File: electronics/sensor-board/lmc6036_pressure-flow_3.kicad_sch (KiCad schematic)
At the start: 13 parts

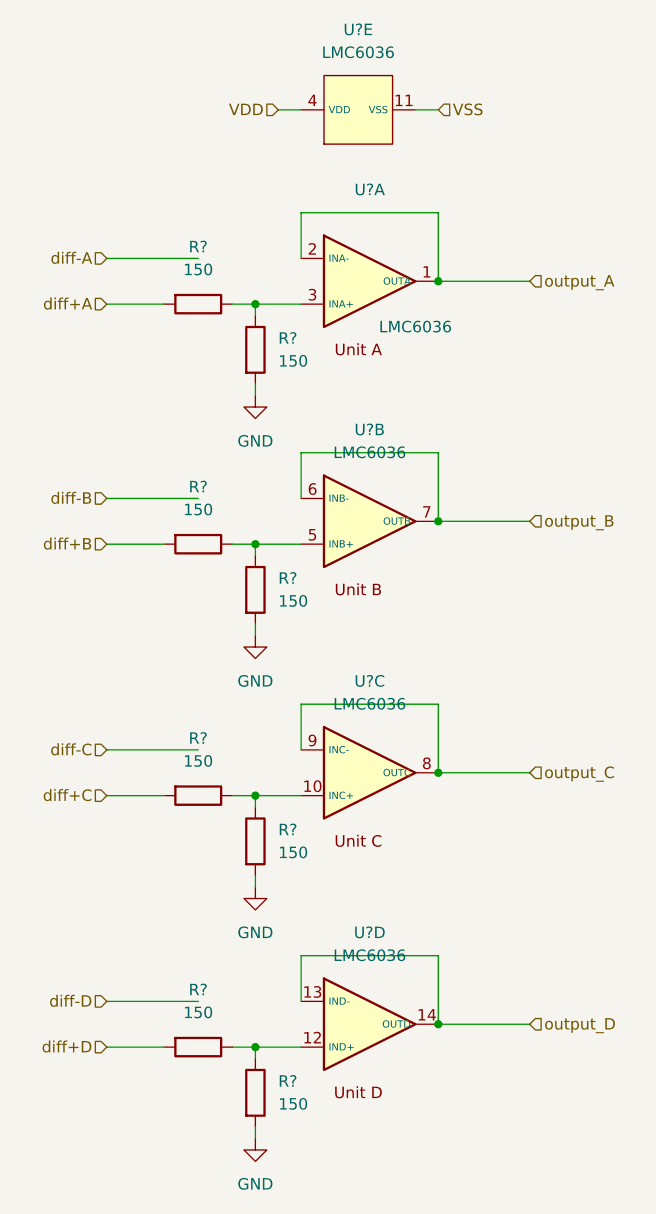
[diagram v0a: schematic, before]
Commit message: work on sensor-board
added MCP960 footprint
finished MCP960 array schematic
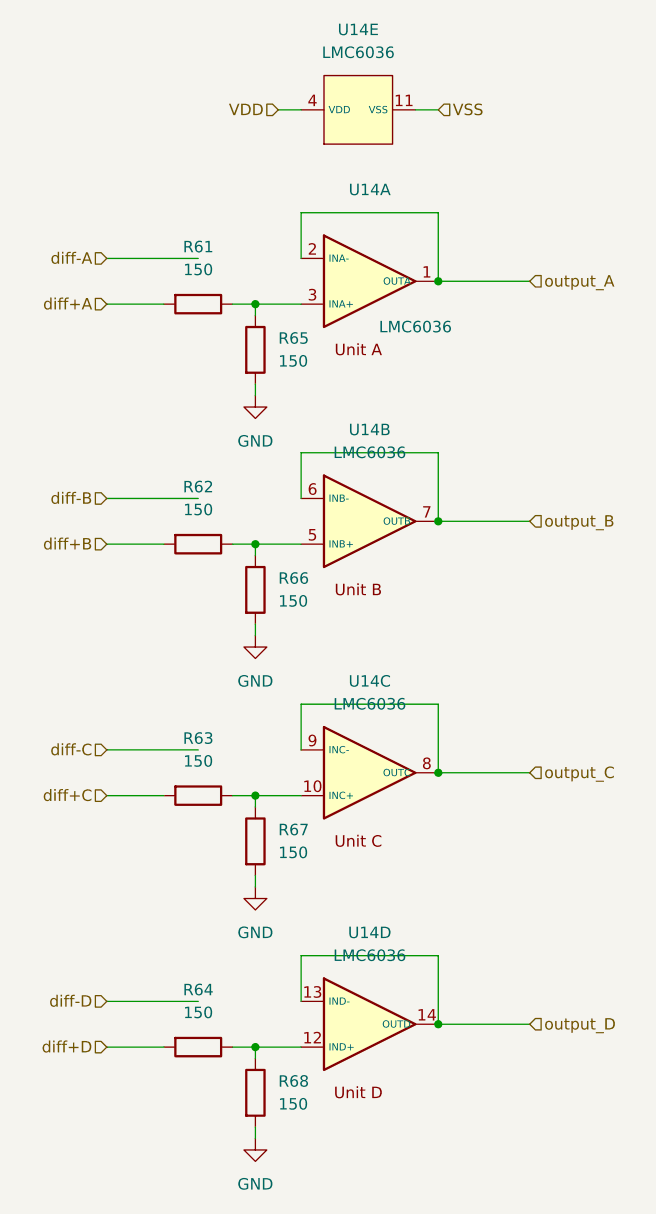
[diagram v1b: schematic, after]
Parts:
- removed R? (x8): 150, symbol Device:R
- removed U? (x5): LMC6036, LMC6036:SOP65P640X120-14N, symbol LMC6036_custom:LMC6036
- added R61, R62, R63, R64, R65, R66, R67, R68: 150, Resistor_SMD:R_0603_1608Metric, symbol Device:R
- added U14: LMC6036, LMC6036:SOP65P640X120-14N, symbol LMC6036_custom:LMC6036
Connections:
- net GND: now also R65.2, R66.2, R67.2, R68.2
- net VDD: now also U14.4 (VDD)
- net VSS: now also U14.11 (VSS)
- net diff+A: now also R61.2
- net diff+B: now also R62.2
- net diff+C: now also R63.2
- net diff+D: now also R64.2
- net output_A: now also U14.1 (OUTA), U14.2 (INA-)
- net output_B: now also U14.6 (INB-), U14.7 (OUTB)
- net output_C: now also U14.8 (OUTC), U14.9 (INC-)
- net output_D: now also U14.13 (IND-), U14.14 (OUTD)
- new net: R62.1, R66.1, U14.5 (INB+)
- new net: R64.1, R68.1, U14.12 (IND+)
- new net: R63.1, R67.1, U14.10 (INC+)
- new net: R61.1, R65.1, U14.3 (INA+)
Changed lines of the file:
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@@
   (symbol (lib_id "power:GND") (at 142.24 76.2 0) (unit 1)
     (in_bom yes) (on_board yes) (fields_autoplaced)
-    (property "Reference" "#PWR?" (id 0) (at 142.24 82.55 0)
+    (property "Reference" "#PWR0185" (id 0) (at 142.24 82.55 0)
       (effects (font (size 1.27 1.27)) hide)
     )
@@
   (symbol (lib_id "power:GND") (at 142.24 102.87 0) (unit 1)
     (in_bom yes) (on_board yes) (fields_autoplaced)
-    (property "Reference" "#PWR?" (id 0) (at 142.24 109.22 0)
+    (property "Reference" "#PWR0187" (id 0) (at 142.24 109.22 0)
       (effects (font (size 1.27 1.27)) hide)
     )
@@
   (symbol (lib_id "power:GND") (at 142.24 130.81 0) (unit 1)
     (in_bom yes) (on_board yes) (fields_autoplaced)
-    (property "Reference" "#PWR?" (id 0) (at 142.24 137.16 0)
+    (property "Reference" "#PWR0186" (id 0) (at 142.24 137.16 0)
       (effects (font (size 1.27 1.27)) hide)
     )
@@
   (symbol (lib_id "power:GND") (at 142.24 158.75 0) (unit 1)
     (in_bom yes) (on_board yes) (fields_autoplaced)
-    (property "Reference" "#PWR?" (id 0) (at 142.24 165.1 0)
+    (property "Reference" "#PWR0188" (id 0) (at 142.24 165.1 0)
       (effects (font (size 1.27 1.27)) hide)
     )
@@
   (symbol (lib_id "Device:R") (at 135.89 66.04 270) (unit 1)
     (in_bom yes) (on_board yes) (fields_autoplaced)
-    (property "Reference" "R?" (id 0) (at 135.89 59.69 90))
+    (property "Reference" "R61" (id 0) (at 135.89 59.69 90))
     (property "Value" "150" (id 1) (at 135.89 62.23 90))
-    (property "Footprint" "" (id 2) (at 135.89 64.262 90)
+    (property "Footprint" "Resistor_SMD:R_0603_1608Metric" (id 2) (at 135.89 64.262 90)
       (effects (font (size 1.27 1.27)) hide)
     )
@@
   (symbol (lib_id "Device:R") (at 135.89 92.71 270) (unit 1)
     (in_bom yes) (on_board yes) (fields_autoplaced)
-    (property "Reference" "R?" (id 0) (at 135.89 86.36 90))
+    (property "Reference" "R62" (id 0) (at 135.89 86.36 90))
     (property "Value" "150" (id 1) (at 135.89 88.9 90))
-    (property "Footprint" "" (id 2) (at 135.89 90.932 90)
+    (property "Footprint" "Resistor_SMD:R_0603_1608Metric" (id 2) (at 135.89 90.932 90)
       (effects (font (size 1.27 1.27)) hide)
     )
@@
   (symbol (lib_id "Device:R") (at 135.89 120.65 270) (unit 1)
     (in_bom yes) (on_board yes) (fields_autoplaced)
-    (property "Reference" "R?" (id 0) (at 135.89 114.3 90))
+    (property "Reference" "R63" (id 0) (at 135.89 114.3 90))
     (property "Value" "150" (id 1) (at 135.89 116.84 90))
-    (property "Footprint" "" (id 2) (at 135.89 118.872 90)
+    (property "Footprint" "Resistor_SMD:R_0603_1608Metric" (id 2) (at 135.89 118.872 90)
       (effects (font (size 1.27 1.27)) hide)
     )
@@
   (symbol (lib_id "Device:R") (at 135.89 148.59 270) (unit 1)
     (in_bom yes) (on_board yes) (fields_autoplaced)
-    (property "Reference" "R?" (id 0) (at 135.89 142.24 90))
+    (property "Reference" "R64" (id 0) (at 135.89 142.24 90))
     (property "Value" "150" (id 1) (at 135.89 144.78 90))
-    (property "Footprint" "" (id 2) (at 135.89 146.812 90)
+    (property "Footprint" "Resistor_SMD:R_0603_1608Metric" (id 2) (at 135.89 146.812 90)
       (effects (font (size 1.27 1.27)) hide)
     )
@@
   (symbol (lib_id "Device:R") (at 142.24 71.12 0) (unit 1)
     (in_bom yes) (on_board yes) (fields_autoplaced)
-    (property "Reference" "R?" (id 0) (at 144.78 69.8499 0)
+    (property "Reference" "R65" (id 0) (at 144.78 69.8499 0)
       (effects (font (size 1.27 1.27)) (justify left))
     )
@@
       (effects (font (size 1.27 1.27)) (justify left))
     )
-    (property "Footprint" "" (id 2) (at 140.462 71.12 90)
+    (property "Footprint" "Resistor_SMD:R_0603_1608Metric" (id 2) (at 140.462 71.12 90)
       (effects (font (size 1.27 1.27)) hide)
     )
@@
   (symbol (lib_id "Device:R") (at 142.24 97.79 0) (unit 1)
     (in_bom yes) (on_board yes) (fields_autoplaced)
-    (property "Reference" "R?" (id 0) (at 144.78 96.5199 0)
+    (property "Reference" "R66" (id 0) (at 144.78 96.5199 0)
       (effects (font (size 1.27 1.27)) (justify left))
     )
@@
       (effects (font (size 1.27 1.27)) (justify left))
     )
-    (property "Footprint" "" (id 2) (at 140.462 97.79 90)
+    (property "Footprint" "Resistor_SMD:R_0603_1608Metric" (id 2) (at 140.462 97.79 90)
       (effects (font (size 1.27 1.27)) hide)
     )
@@
   (symbol (lib_id "Device:R") (at 142.24 125.73 0) (unit 1)
     (in_bom yes) (on_board yes) (fields_autoplaced)
-    (property "Reference" "R?" (id 0) (at 144.78 124.4599 0)
+    (property "Reference" "R67" (id 0) (at 144.78 124.4599 0)
       (effects (font (size 1.27 1.27)) (justify left))
     )
@@
       (effects (font (size 1.27 1.27)) (justify left))
     )
-    (property "Footprint" "" (id 2) (at 140.462 125.73 90)
+    (property "Footprint" "Resistor_SMD:R_0603_1608Metric" (id 2) (at 140.462 125.73 90)
       (effects (font (size 1.27 1.27)) hide)
     )
@@
   (symbol (lib_id "Device:R") (at 142.24 153.67 0) (unit 1)
     (in_bom yes) (on_board yes) (fields_autoplaced)
-    (property "Reference" "R?" (id 0) (at 144.78 152.3999 0)
+    (property "Reference" "R68" (id 0) (at 144.78 152.3999 0)
       (effects (font (size 1.27 1.27)) (justify left))
     )
@@
       (effects (font (size 1.27 1.27)) (justify left))
     )
-    (property "Footprint" "" (id 2) (at 140.462 153.67 90)
+    (property "Footprint" "Resistor_SMD:R_0603_1608Metric" (id 2) (at 140.462 153.67 90)
       (effects (font (size 1.27 1.27)) hide)
     )
@@
   (symbol (lib_id "LMC6036_custom:LMC6036") (at 153.67 44.45 90) (unit 5)
     (in_bom yes) (on_board yes) (fields_autoplaced)
-    (property "Reference" "U?" (id 0) (at 153.67 35.56 90))
+    (property "Reference" "U14" (id 0) (at 153.67 35.56 90))
     (property "Value" "LMC6036" (id 1) (at 153.67 38.1 90))
     (property "Footprint" "LMC6036:SOP65P640X120-14N" (id 2) (at 153.67 42.545 0)
@@
   (symbol (lib_id "LMC6036_custom:LMC6036") (at 153.67 63.5 0) (unit 1)
     (in_bom yes) (on_board yes)
-    (property "Reference" "U?" (id 0) (at 154.94 53.34 0))
+    (property "Reference" "U14" (id 0) (at 154.94 53.34 0))
     (property "Value" "LMC6036" (id 1) (at 160.02 68.58 0))
     (property "Footprint" "LMC6036:SOP65P640X120-14N" (id 2) (at 155.575 63.5 0)
@@
   (symbol (lib_id "LMC6036_custom:LMC6036") (at 153.67 90.17 0) (unit 2)
     (in_bom yes) (on_board yes) (fields_autoplaced)
-    (property "Reference" "U?" (id 0) (at 154.94 80.01 0))
+    (property "Reference" "U14" (id 0) (at 154.94 80.01 0))
     (property "Value" "LMC6036" (id 1) (at 154.94 82.55 0))
     (property "Footprint" "LMC6036:SOP65P640X120-14N" (id 2) (at 155.575 90.17 0)
@@
   (symbol (lib_id "LMC6036_custom:LMC6036") (at 153.67 118.11 0) (unit 3)
     (in_bom yes) (on_board yes) (fields_autoplaced)
-    (property "Reference" "U?" (id 0) (at 154.94 107.95 0))
+    (property "Reference" "U14" (id 0) (at 154.94 107.95 0))
     (property "Value" "LMC6036" (id 1) (at 154.94 110.49 0))
     (property "Footprint" "LMC6036:SOP65P640X120-14N" (id 2) (at 155.575 118.11 0)
@@
   (symbol (lib_id "LMC6036_custom:LMC6036") (at 153.67 146.05 0) (unit 4)
     (in_bom yes) (on_board yes) (fields_autoplaced)
-    (property "Reference" "U?" (id 0) (at 154.94 135.89 0))
+    (property "Reference" "U14" (id 0) (at 154.94 135.89 0))
     (property "Value" "LMC6036" (id 1) (at 154.94 138.43 0))
     (property "Footprint" "LMC6036:SOP65P640X120-14N" (id 2) (at 155.575 146.05 0)

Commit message: Finalized sensor-board schematic
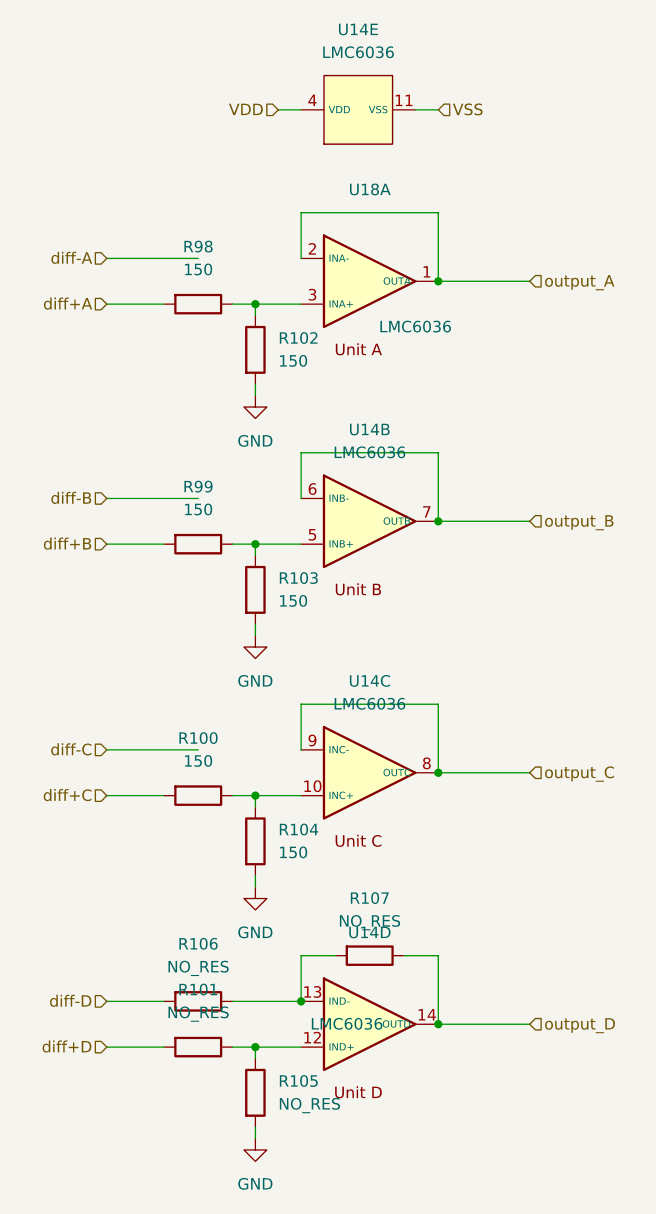
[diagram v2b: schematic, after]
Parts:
- added R106, R107: NO_RES, Resistor_SMD:R_0603_1608Metric, symbol Device:R
- R101: renamed from R64; value 150 -> NO_RES
- R105: renamed from R68; value 150 -> NO_RES
- renumbered R63 to R100, R65 to R102, R66 to R103, R67 to R104, R61 to R98, R62 to R99, U14 to U18
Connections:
- net diff-D: now also R106.2
- net output_D: now also R107.1; no longer U14.13 (IND-)
- new net: R106.1, R107.2, U14.13 (IND-)
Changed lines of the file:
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@@
   (junction (at 142.24 120.65) (diameter 0) (color 0 0 0 0))
   (junction (at 142.24 148.59) (diameter 0) (color 0 0 0 0))
+  (junction (at 147.32 143.51) (diameter 0) (color 0 0 0 0))
   (junction (at 162.56 63.5) (diameter 0) (color 0 0 0 0))
   (junction (at 162.56 90.17) (diameter 0) (color 0 0 0 0))
@@
     (stroke (width 0) (type default) (color 0 0 0 0))
   )
-  (wire (pts (xy 125.73 143.51) (xy 135.89 143.51))
+  (wire (pts (xy 125.73 143.51) (xy 132.08 143.51))
     (stroke (width 0) (type default) (color 0 0 0 0))
   )
@@
     (stroke (width 0) (type default) (color 0 0 0 0))
   )
+  (wire (pts (xy 139.7 143.51) (xy 147.32 143.51))
+    (stroke (width 0) (type default) (color 0 0 0 0))
+  )
   (wire (pts (xy 139.7 148.59) (xy 142.24 148.59))
     (stroke (width 0) (type default) (color 0 0 0 0))
@@
     (stroke (width 0) (type default) (color 0 0 0 0))
   )
-  (wire (pts (xy 147.32 138.43) (xy 162.56 138.43))
+  (wire (pts (xy 147.32 138.43) (xy 151.13 138.43))
+    (stroke (width 0) (type default) (color 0 0 0 0))
+  )
+  (wire (pts (xy 158.75 138.43) (xy 162.56 138.43))
     (stroke (width 0) (type default) (color 0 0 0 0))
   )
@@
   (symbol (lib_id "power:GND") (at 142.24 76.2 0) (unit 1)
     (in_bom yes) (on_board yes) (fields_autoplaced)
-    (property "Reference" "#PWR0185" (id 0) (at 142.24 82.55 0)
+    (property "Reference" "#PWR0131" (id 0) (at 142.24 82.55 0)
       (effects (font (size 1.27 1.27)) hide)
     )
@@
   (symbol (lib_id "power:GND") (at 142.24 102.87 0) (unit 1)
     (in_bom yes) (on_board yes) (fields_autoplaced)
-    (property "Reference" "#PWR0187" (id 0) (at 142.24 109.22 0)
+    (property "Reference" "#PWR0132" (id 0) (at 142.24 109.22 0)
       (effects (font (size 1.27 1.27)) hide)
     )
@@
   (symbol (lib_id "power:GND") (at 142.24 130.81 0) (unit 1)
     (in_bom yes) (on_board yes) (fields_autoplaced)
-    (property "Reference" "#PWR0186" (id 0) (at 142.24 137.16 0)
+    (property "Reference" "#PWR0133" (id 0) (at 142.24 137.16 0)
       (effects (font (size 1.27 1.27)) hide)
     )
@@
   (symbol (lib_id "power:GND") (at 142.24 158.75 0) (unit 1)
     (in_bom yes) (on_board yes) (fields_autoplaced)
-    (property "Reference" "#PWR0188" (id 0) (at 142.24 165.1 0)
+    (property "Reference" "#PWR0134" (id 0) (at 142.24 165.1 0)
       (effects (font (size 1.27 1.27)) hide)
     )
@@
   (symbol (lib_id "Device:R") (at 135.89 66.04 270) (unit 1)
     (in_bom yes) (on_board yes) (fields_autoplaced)
-    (property "Reference" "R61" (id 0) (at 135.89 59.69 90))
+    (property "Reference" "R98" (id 0) (at 135.89 59.69 90))
     (property "Value" "150" (id 1) (at 135.89 62.23 90))
     (property "Footprint" "Resistor_SMD:R_0603_1608Metric" (id 2) (at 135.89 64.262 90)
@@
   (symbol (lib_id "Device:R") (at 135.89 92.71 270) (unit 1)
     (in_bom yes) (on_board yes) (fields_autoplaced)
-    (property "Reference" "R62" (id 0) (at 135.89 86.36 90))
+    (property "Reference" "R99" (id 0) (at 135.89 86.36 90))
     (property "Value" "150" (id 1) (at 135.89 88.9 90))
     (property "Footprint" "Resistor_SMD:R_0603_1608Metric" (id 2) (at 135.89 90.932 90)
@@
   (symbol (lib_id "Device:R") (at 135.89 120.65 270) (unit 1)
     (in_bom yes) (on_board yes) (fields_autoplaced)
-    (property "Reference" "R63" (id 0) (at 135.89 114.3 90))
+    (property "Reference" "R100" (id 0) (at 135.89 114.3 90))
     (property "Value" "150" (id 1) (at 135.89 116.84 90))
     (property "Footprint" "Resistor_SMD:R_0603_1608Metric" (id 2) (at 135.89 118.872 90)
@@
     (pin "2")
   )
+  (symbol (lib_id "Device:R") (at 135.89 143.51 270) (unit 1)
+    (in_bom yes) (on_board yes) (fields_autoplaced)
+    (property "Reference" "R106" (id 0) (at 135.89 137.16 90))
+    (property "Value" "NO_RES" (id 1) (at 135.89 139.7 90))
+    (property "Footprint" "Resistor_SMD:R_0603_1608Metric" (id 2) (at 135.89 141.732 90)
+      (effects (font (size 1.27 1.27)) hide)
+    )
+    (property "Datasheet" "~" (id 3) (at 135.89 143.51 0)
+      (effects (font (size 1.27 1.27)) hide)
+    )
+    (pin "1")
+    (pin "2")
+  )
   (symbol (lib_id "Device:R") (at 135.89 148.59 270) (unit 1)
     (in_bom yes) (on_board yes) (fields_autoplaced)
-    (property "Reference" "R64" (id 0) (at 135.89 142.24 90))
-    (property "Value" "150" (id 1) (at 135.89 144.78 90))
+    (property "Reference" "R101" (id 0) (at 135.89 142.24 90))
+    (property "Value" "NO_RES" (id 1) (at 135.89 144.78 90))
     (property "Footprint" "Resistor_SMD:R_0603_1608Metric" (id 2) (at 135.89 146.812 90)
       (effects (font (size 1.27 1.27)) hide)
@@
   (symbol (lib_id "Device:R") (at 142.24 71.12 0) (unit 1)
     (in_bom yes) (on_board yes) (fields_autoplaced)
-    (property "Reference" "R65" (id 0) (at 144.78 69.8499 0)
+    (property "Reference" "R102" (id 0) (at 144.78 69.8499 0)
       (effects (font (size 1.27 1.27)) (justify left))
     )
@@
   (symbol (lib_id "Device:R") (at 142.24 97.79 0) (unit 1)
     (in_bom yes) (on_board yes) (fields_autoplaced)
-    (property "Reference" "R66" (id 0) (at 144.78 96.5199 0)
+    (property "Reference" "R103" (id 0) (at 144.78 96.5199 0)
       (effects (font (size 1.27 1.27)) (justify left))
     )
@@
   (symbol (lib_id "Device:R") (at 142.24 125.73 0) (unit 1)
     (in_bom yes) (on_board yes) (fields_autoplaced)
-    (property "Reference" "R67" (id 0) (at 144.78 124.4599 0)
+    (property "Reference" "R104" (id 0) (at 144.78 124.4599 0)
       (effects (font (size 1.27 1.27)) (justify left))
     )
@@
   (symbol (lib_id "Device:R") (at 142.24 153.67 0) (unit 1)
     (in_bom yes) (on_board yes) (fields_autoplaced)
-    (property "Reference" "R68" (id 0) (at 144.78 152.3999 0)
-      (effects (font (size 1.27 1.27)) (justify left))
-    )
-    (property "Value" "150" (id 1) (at 144.78 154.9399 0)
+    (property "Reference" "R105" (id 0) (at 144.78 152.3999 0)
+      (effects (font (size 1.27 1.27)) (justify left))
+    )
+    (property "Value" "NO_RES" (id 1) (at 144.78 154.9399 0)
       (effects (font (size 1.27 1.27)) (justify left))
     )
@@
     )
     (property "Datasheet" "~" (id 3) (at 142.24 153.67 0)
+      (effects (font (size 1.27 1.27)) hide)
+    )
+    (pin "1")
+    (pin "2")
+  )
+  (symbol (lib_id "Device:R") (at 154.94 138.43 270) (unit 1)
+    (in_bom yes) (on_board yes) (fields_autoplaced)
+    (property "Reference" "R107" (id 0) (at 154.94 132.08 90))
+    (property "Value" "NO_RES" (id 1) (at 154.94 134.62 90))
+    (property "Footprint" "Resistor_SMD:R_0603_1608Metric" (id 2) (at 154.94 136.652 90)
+      (effects (font (size 1.27 1.27)) hide)
+    )
+    (property "Datasheet" "~" (id 3) (at 154.94 138.43 0)
       (effects (font (size 1.27 1.27)) hide)
     )
@@
   (symbol (lib_id "LMC6036_custom:LMC6036") (at 153.67 63.5 0) (unit 1)
     (in_bom yes) (on_board yes)
-    (property "Reference" "U14" (id 0) (at 154.94 53.34 0))
+    (property "Reference" "U18" (id 0) (at 154.94 53.34 0))
     (property "Value" "LMC6036" (id 1) (at 160.02 68.58 0))
     (property "Footprint" "LMC6036:SOP65P640X120-14N" (id 2) (at 155.575 63.5 0)
@@
   )
   (symbol (lib_id "LMC6036_custom:LMC6036") (at 153.67 146.05 0) (unit 4)
-    (in_bom yes) (on_board yes) (fields_autoplaced)
+    (in_bom yes) (on_board yes)
     (property "Reference" "U14" (id 0) (at 154.94 135.89 0))
-    (property "Value" "LMC6036" (id 1) (at 154.94 138.43 0))
+    (property "Value" "LMC6036" (id 1) (at 152.4 146.05 0))
     (property "Footprint" "LMC6036:SOP65P640X120-14N" (id 2) (at 155.575 146.05 0)
       (effects (font (size 1.27 1.27)) hide)
